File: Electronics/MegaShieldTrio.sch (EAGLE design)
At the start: 56 parts, among them X1 Vehicle control, X2 2odo__, X3 1odo__, X4 RJ45-8L-B, X5 RJ45-8L-B

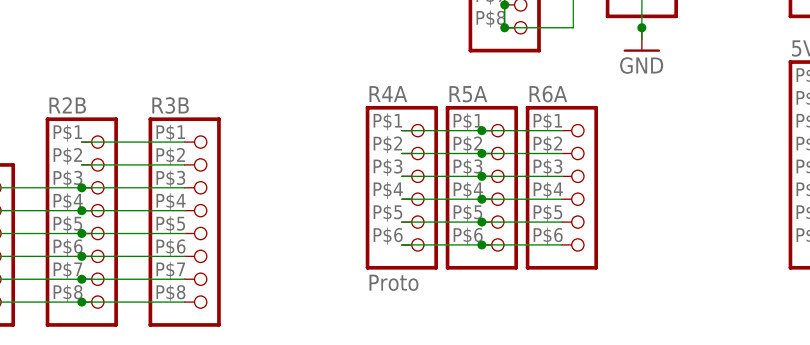
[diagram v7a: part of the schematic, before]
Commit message: Silkscreens; smaller sonar board
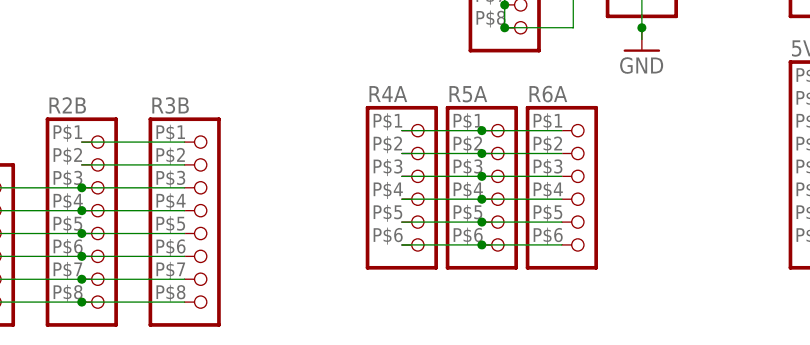
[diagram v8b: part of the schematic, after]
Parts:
- R4A: value Proto -> (none)
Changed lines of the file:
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@@
 <part name="R3B" library="Elcano" deviceset="PINHD-1X8" device="SMALL8"/>
 <part name="R1B" library="Elcano" deviceset="1X6HEADER" device="" value=" "/>
-<part name="R4A" library="Elcano" deviceset="1X6HEADER" device="" value="Proto"/>
+<part name="R4A" library="Elcano" deviceset="1X6HEADER" device="" value=" "/>
 <part name="R5A" library="Elcano" deviceset="1X6HEADER" device="" value=" "/>
 <part name="R6A" library="Elcano" deviceset="1X6HEADER" device="" value=""/>
